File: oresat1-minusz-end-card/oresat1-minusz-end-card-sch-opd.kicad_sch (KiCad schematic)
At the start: 59 parts, among them Q1 DMP2240UDM, Q2 PMV45EN, Q3 PMV45EN, Q4 PMV45EN, Q5 DMP2240UDM-7, Q6 PMV45EN, Q7 DMP2240UDM-7, U11 MIC842LYC5, U12 MIC842LYC5, U2 MAX7310, U201 TS5A21366, U202 TS5A21366, U203 TS5A21366, U204 TS5A21366

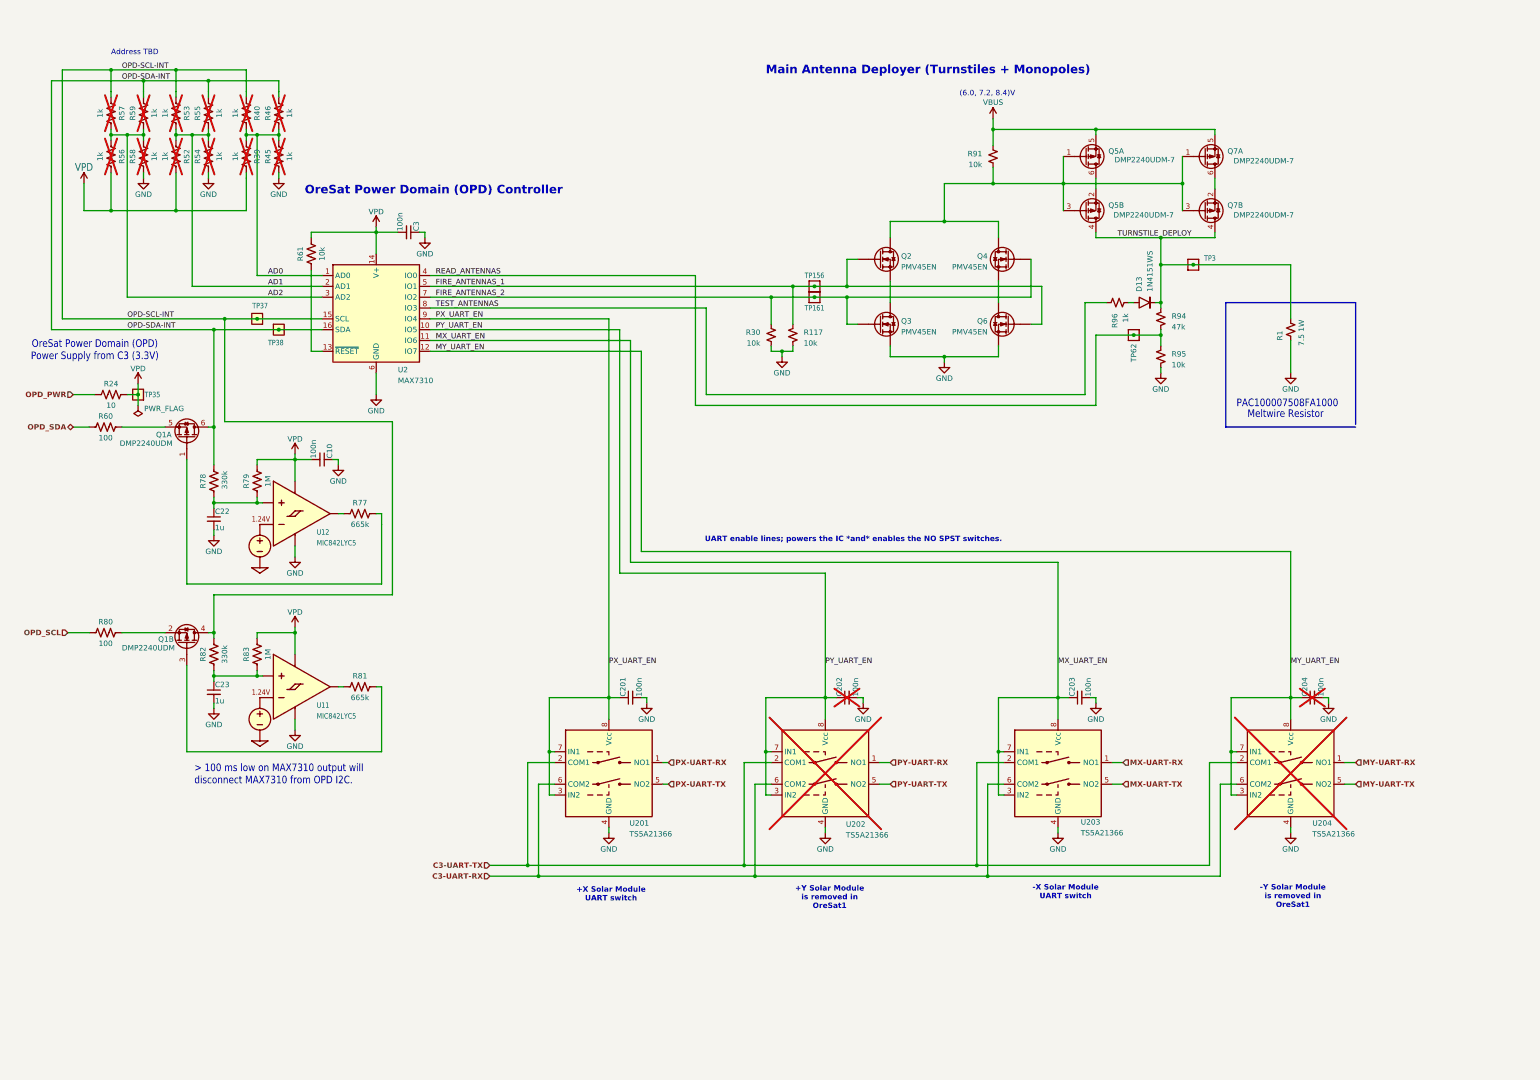
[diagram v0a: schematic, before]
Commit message: Changes to minus Z
Resolved 2 git issues. Added led test light to deployer circuit to test deployment
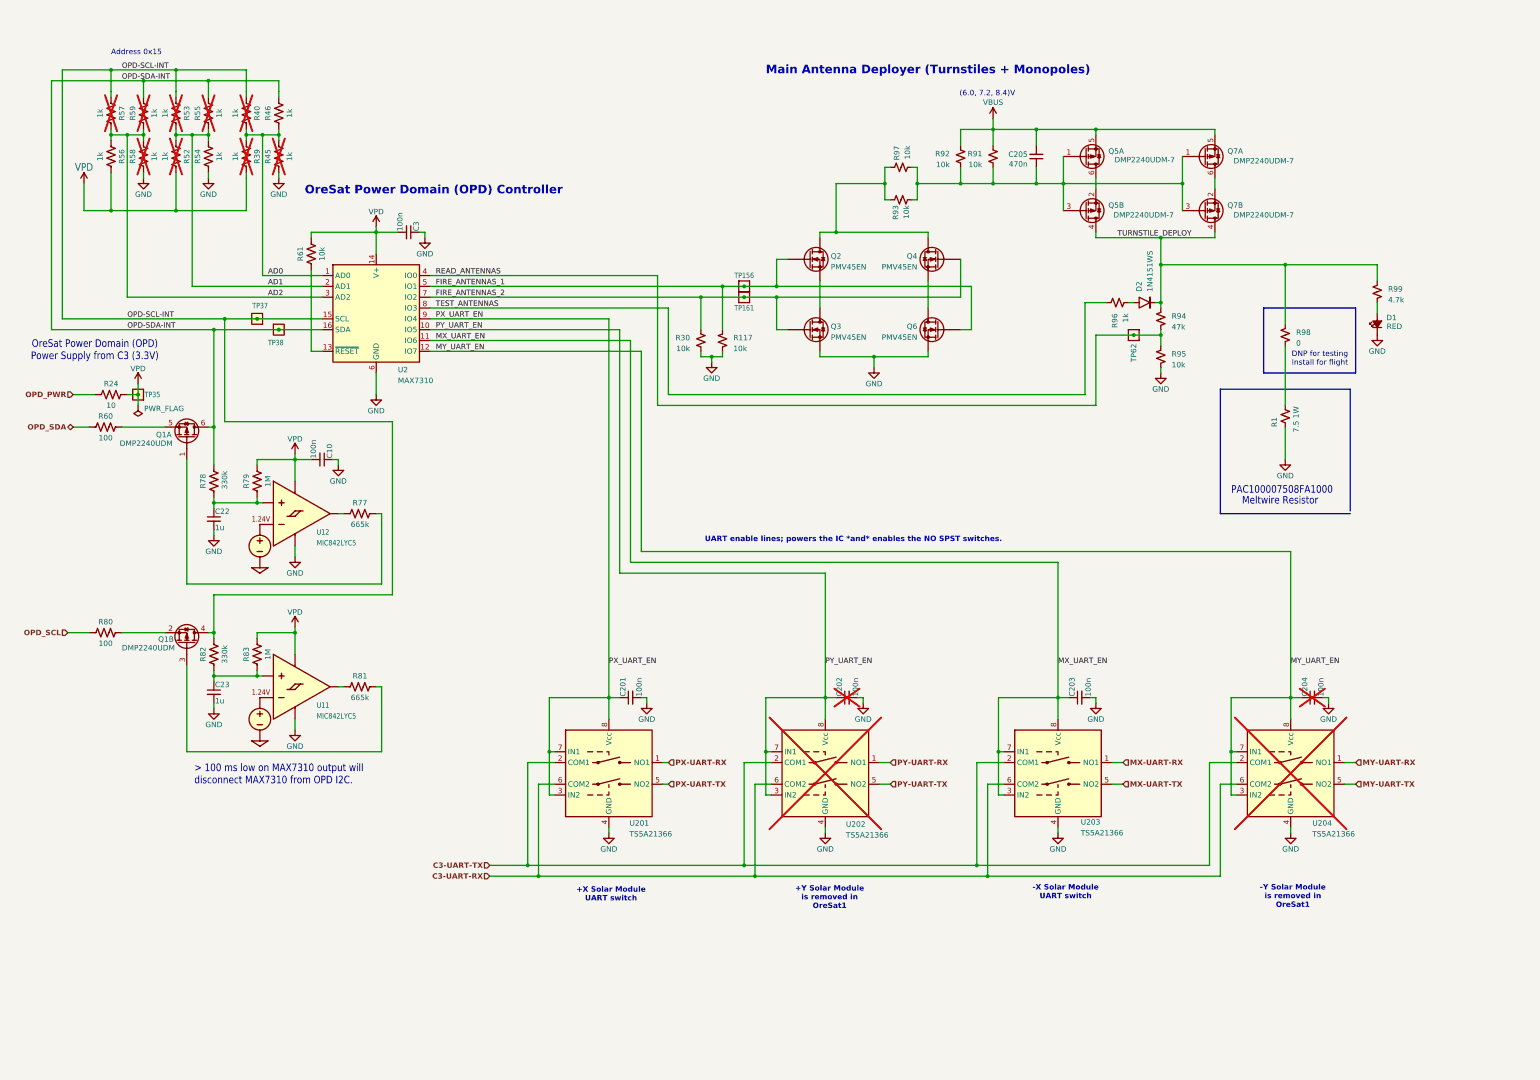
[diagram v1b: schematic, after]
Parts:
- removed TP3: Test-Point, oresat-misc:TestPoint_Pad_D1.0mm, symbol oresat-misc:Test-Point-1mm-round
- added C205: 470n, oresat-passives:0603-C-NOSILK, symbol Device:C_Small
- added D1: RED, LED_SMD:LED_0603_1608Metric, symbol Device:LED_Small_Filled
- added R92, R93, R97: 10k, oresat-passives:0603-C-NOSILK, symbol Device:R_Small_US
- added R98: 0, oresat-passives:1206-C, symbol Device:R_Small_US
- added R99: 4.7k, oresat-passives:0603-C-NOSILK, symbol Device:R_Small_US
- R46, R54, R56: now fitted
- renumbered D13 to D2
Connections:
- net GND: now also D1.1 (K)
- net TURNSTILE_DEPLOY: now also R98.1, R99.1; no longer R1.1
- net VBUS: now also C205.2, R92.1
- net at Q5.1 (G), Q5.3 (G), Q7.1 (G)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: now also C205.1, R92.2, R93.2, R97.2; no longer Q2.3 (D), Q4.3 (D)
- new net: Q2.3 (D), Q4.3 (D), R93.1, R97.1
- new net: D1.2 (A), R99.2
- new net: R1.1, R98.2
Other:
- note added: "Address 0x15"
- note added: "DNP for testing Install for flight"
- note removed: "Address TBD"
- moved on the sheet: Q2, Q3, Q4, Q6, R1, R117, R30, TP156, TP161

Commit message: Routine push
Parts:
- removed C202, C204: 100n, oresat-passives:0603-C-NOSILK, symbol Device:C_Small
- removed U202, U204: TS5A21366, Package_SO:VSSOP-8_2.3x2mm_P0.5mm, symbol oresat-ics:TS5A21366
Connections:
- net MY_UART_EN: no longer names the net of U2.12 (IO7)
- net PY_UART_EN: no longer names the net of U2.10 (IO5)
- no-connect marks 0 -> 2
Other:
- moved on the sheet: C203, C205, D1, D2, Q5A, Q5B, Q7A, Q7B, R1, R91, R92, R93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

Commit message: Lots of little polishing, checking rules, updating symbols and footprints, adding README and Makefile
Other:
- note added: ""DEPLOY""
- note added: "1206"
- moved on the sheet: D1, R1, R98, R99

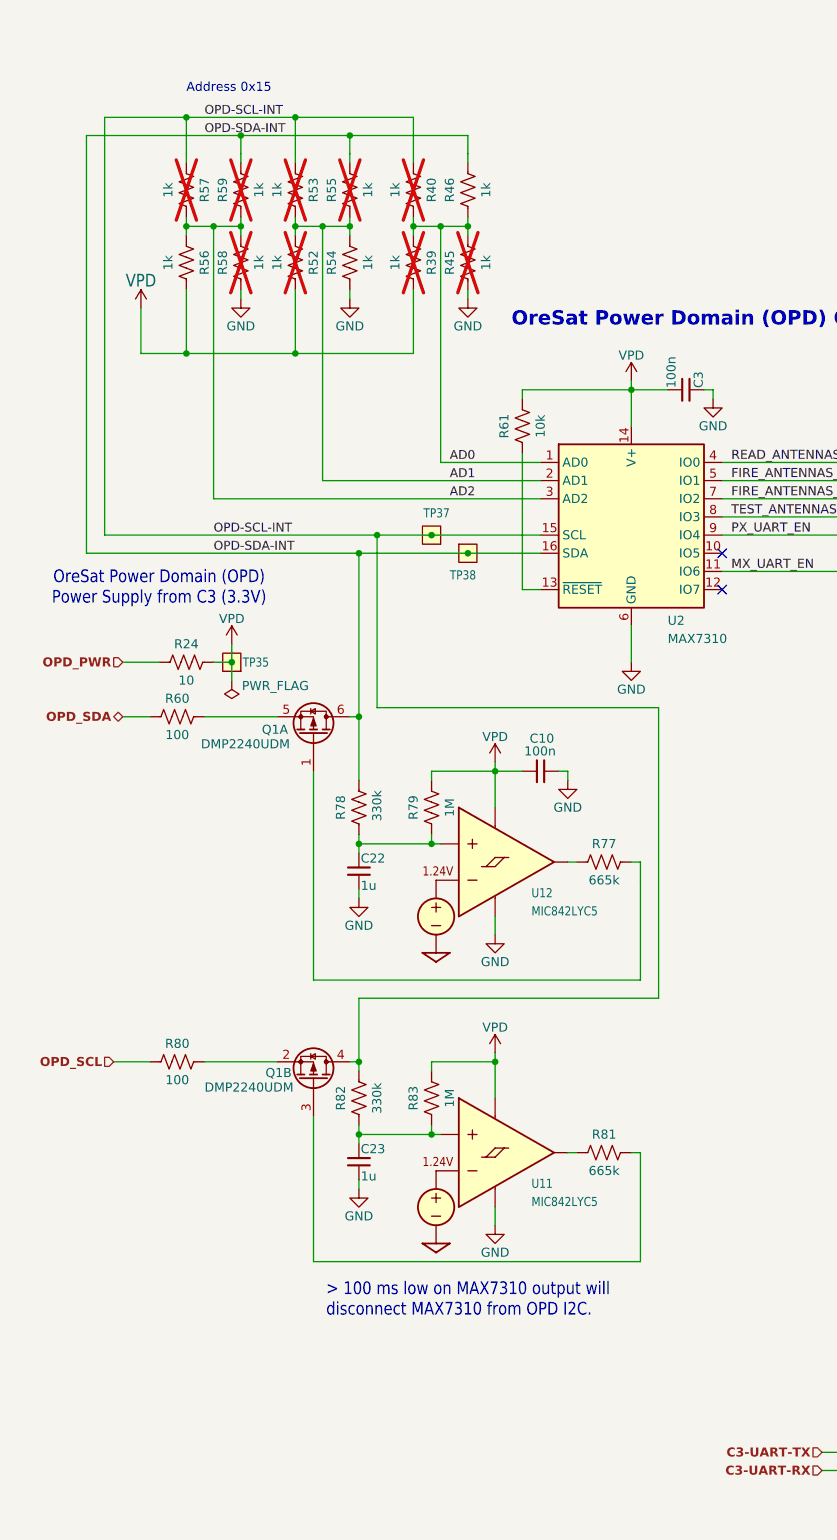
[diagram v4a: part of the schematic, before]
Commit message: Feedback from Pete: add opd_pwr cap, make consistent with +Z end card
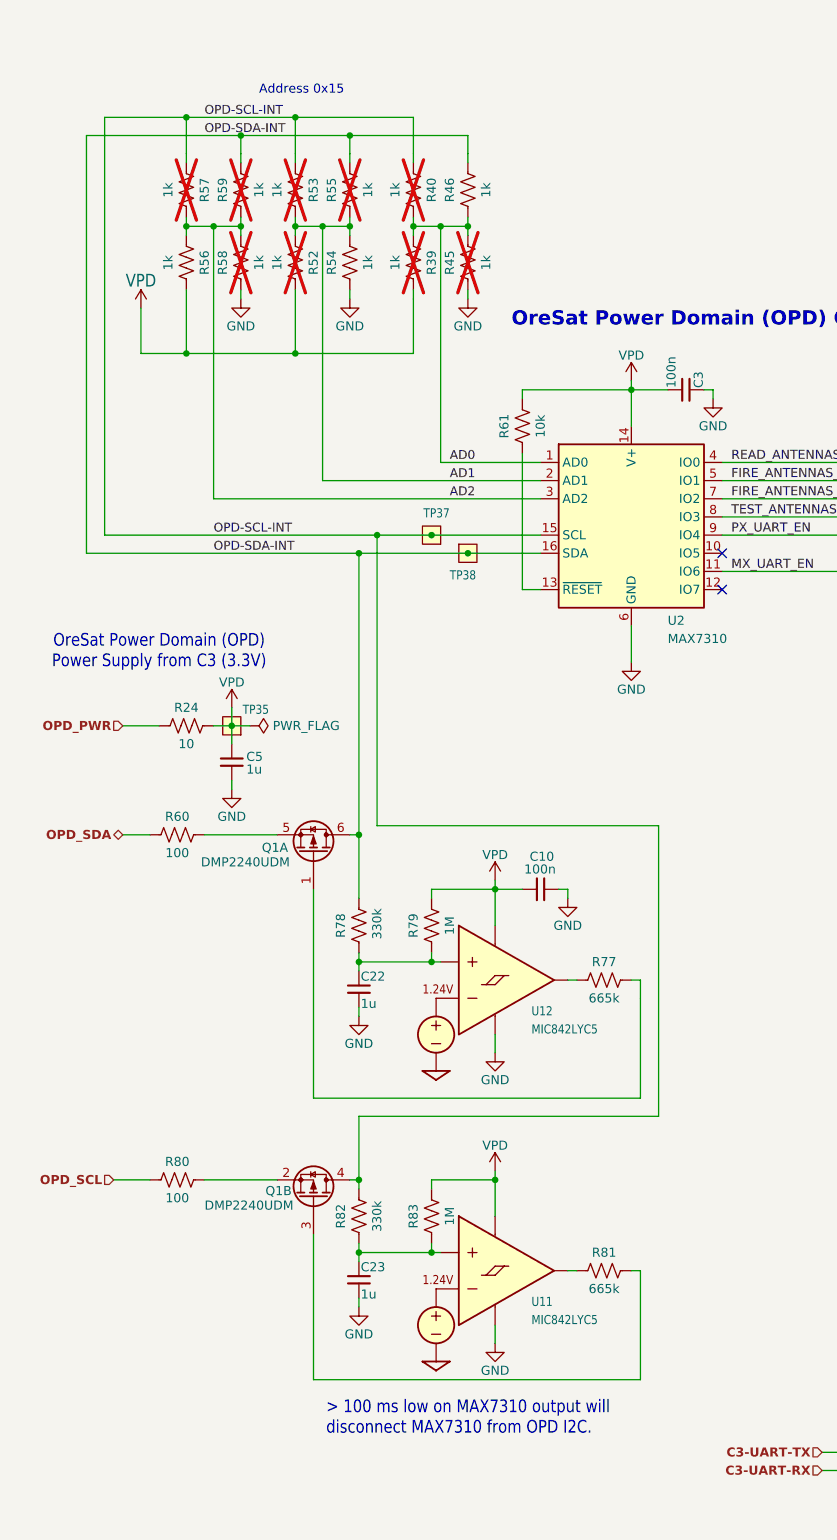
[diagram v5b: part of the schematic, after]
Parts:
- added C5: 1u, oresat-passives:0603-C-NOSILK, symbol Device:C_Small
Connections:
- net GND: now also C5.2
- net VPD: now also C5.1
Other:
- moved on the sheet: C10, C22, C23, Q1A, Q1B, R24, R60, R77, R78, R79, R80, R81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

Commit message: V1.4 of the -Z end card. Better ground stitching, cleanup, good to go
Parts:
- added TP157, TP158, TP159: Test-Point, oresat-misc:TestPoint_Pad_D1.0mm, symbol oresat-misc:Test-Point-1mm-round
- C205: value 470n -> 1u; DPN 399-C0603C474K3RACAUTOCT-ND -> 490-GRT188R71E105KE13DCT-ND; MFR KEMET -> Murata Electronics; MPN C0603C474K3RACAUTO -> GRT188R71E105KE13D
- Q1: value DMP2240UDM -> DMP2240UDM-7; MPN DMP2240UDM -> DMP2240UDM-7
- Q2, Q3, Q4, Q6: value PMV45EN -> DMN2053UQ-13; DIS Digi-Key -> DigiKey; DPN 1727-2307-1-ND -> 31-DMN2053UQ-13CT-ND; MFR Nexperia -> Diodes Incorporated; MPN PMV45EN2R -> DMN2053UQ-13
- Q5, Q7: MPN DMP2240UDM -> DMP2240UDM-7
- R39, R40, R45, R52, R53, R55, R57, R58, R59: value 1k -> 100
- R46, R54, R56: value 1k -> 100; DPN RMCF0603FT2K70CT-ND -> RMCF0603FT100RCT-ND; MPN RMCF0603FT1K00 -> RMCF0603FT100R
- R99: value 4.7k -> 1k; DPN RMCF0603FT4K70CT-ND -> RMCF0603FT2K70CT-ND; MPN RMCF0603FT4K70 -> RMCF0603FT1K00
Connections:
- net at C205.1, Q5.1 (G), Q5.3 (G)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: now also TP157.1
- net at U2.10 (IO5): now also TP158.1
- net at U2.12 (IO7): now also TP159.1
- no-connect marks 2 -> 0
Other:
- note added: "All resistors are 0603 1% AEC-Q200 unless marked. All capacitors are 0603 AEC-Q200 Vw >= 16V X5R or better unless marked."
- moved on the sheet: C10, C201, C203, C205, C22, C23, C3, C5, D1, D2, Q1A, Q1B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
